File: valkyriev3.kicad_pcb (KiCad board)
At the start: 4 copper layers, 5 parts, among them J1 USB_C_Receptacle_USB2.0_16P, SW1 SW_SPST, SW2 SW_SPST, U1 ESP32-S3-MINI-1U, U2 MAX3232

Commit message: preliminary schematic wired, all footprints assigned, all laid out in PCB editor.
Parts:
- added BAT1: XH311HU-IV07E, Valkyrie_footprints:XH311HU-IV07E, F.Cu at (262.2, 44.2)
- added BZ1: Buzzer, Buzzer_Beeper:Buzzer_12x9.5RM7.6, F.Cu at (41.4, 116.8)
- added C1: 22 uF, Capacitor_SMD:C_0603_1608Metric, F.Cu at (41.7, 39.8)
- added C10: 10 uF, Capacitor_SMD:C_0603_1608Metric, F.Cu at (28.1, 179.7)
- added C11: 0.1 uF, Capacitor_SMD:C_0805_2012Metric, F.Cu at (23.8, 168.4)
- added C12: 0.1 uF, Capacitor_SMD:C_0805_2012Metric, F.Cu at (23.8, 171.4)
- added C13: 0.1 uF, Capacitor_SMD:C_0805_2012Metric, F.Cu at (23.8, 174.5)
- added C14: 0.1 uF, Capacitor_SMD:C_0805_2012Metric, F.Cu at (23.8, 177.5)
- added C15: 0.1 uF, Capacitor_SMD:C_0805_2012Metric, F.Cu at (23.8, 180.5)
- added C16: 0.1 uF, Capacitor_SMD:C_0805_2012Metric, F.Cu at (117.5, 127.1)
- added C17: 22 uF, Capacitor_SMD:C_0201_0603Metric, F.Cu at (109.7, 134.0)
- added C18: 22 uF, Capacitor_SMD:C_0201_0603Metric, F.Cu at (109.7, 135.8)
- added C19: 22 uF, Capacitor_SMD:C_0603_1608Metric, F.Cu at (115.9, 154.0)
- added C2: 22 uF, Capacitor_SMD:C_0603_1608Metric, F.Cu at (41.7, 42.3)
- added C20: 0.1 uF, Capacitor_SMD:C_0805_2012Metric, F.Cu at (120.1, 157.3)
- added C21: 0.1 uF, Capacitor_SMD:C_0805_2012Metric, F.Cu at (120.1, 160.3)
- added C22: 10 uF, Capacitor_SMD:C_0603_1608Metric, F.Cu at (115.9, 156.5)
- added C23: 22 uF, Capacitor_SMD:C_0603_1608Metric, F.Cu at (115.9, 159.0)
- added C24: 22 uF, Capacitor_SMD:C_0805_2012Metric, F.Cu at (105.0, 138.5)
- added C25: 10 uF, Capacitor_SMD:C_0805_2012Metric, F.Cu at (105.0, 141.5)
- added C26: 0.1 uF, Capacitor_SMD:C_0805_2012Metric, F.Cu at (105.0, 144.5)
- added C27: 0.1 uF, Capacitor_SMD:C_0805_2012Metric, F.Cu at (75.0, 174.9)
- added C28: 10 uF, Capacitor_SMD:C_0603_1608Metric, F.Cu at (79.2, 178.8)
- added C29: 0.1 uF, Capacitor_SMD:C_0805_2012Metric, F.Cu at (75.0, 177.9)
- added C3: 10 uF, Capacitor_SMD:C_0603_1608Metric, F.Cu at (41.7, 44.8)
- added C30: 0.1 uF, Capacitor_SMD:C_0805_2012Metric, F.Cu at (257.5, 43.0)
- added C31: 10 uF, Capacitor_SMD:C_0603_1608Metric, F.Cu at (269.3, 25.2)
- added C32: 22 uF, Capacitor_SMD:C_0603_1608Metric, F.Cu at (269.3, 27.8)
- added C33: 0.1 uF, Capacitor_SMD:C_0805_2012Metric, F.Cu at (257.5, 46.1)
- added C34: 220 uF, Capacitor_SMD:CP_Elec_6.3x7.7, F.Cu at (275.6, 83.2)
- added C35: 22 uF, Capacitor_SMD:C_0805_2012Metric, F.Cu at (272.6, 96.3)
- added C36: 10 uF, Capacitor_SMD:C_0603_1608Metric, F.Cu at (276.9, 96.0)
- added C37: 0.1 uF, Capacitor_SMD:C_0805_2012Metric, F.Cu at (272.6, 99.3)
- added C38: 0.1 uF, Capacitor_SMD:C_0805_2012Metric, F.Cu at (263.1, 140.9)
- added C39: 0.1 uF, Capacitor_SMD:C_0805_2012Metric, F.Cu at (263.1, 143.9)
- added C4: 0.1 uF, Capacitor_SMD:C_0805_2012Metric, F.Cu at (37.4, 40.0)
- added C40: 220 uF, Capacitor_SMD:CP_Elec_6.3x7.7, F.Cu at (134.6, 35.6)
- added C41: 220 uF, Capacitor_SMD:CP_Elec_6.3x7.7, F.Cu at (134.6, 43.7)
- added C42: 220 uF, Capacitor_SMD:CP_Elec_6.3x7.7, F.Cu at (134.6, 51.9)
- added C5: 0.1 uF, Capacitor_SMD:C_0805_2012Metric, F.Cu at (101.2, 79.2)
- added C6: 22 uF, Capacitor_SMD:C_0603_1608Metric, F.Cu at (101.1, 83.6)
- added C7: 0.1 uF, Capacitor_SMD:C_0603_1608Metric, F.Cu at (41.7, 49.8)
- added C8: 0.1 uF, Capacitor_SMD:C_0603_1608Metric, F.Cu at (41.7, 52.3)
- added C9: 22 uF, Capacitor_SMD:C_0603_1608Metric, F.Cu at (28.1, 177.2)
- added D1: NUP2105L, Package_TO_SOT_SMD:SOT-23, F.Cu at (22.4, 82.5)
- added D2: LED, LED_SMD:LED_0805_2012Metric, F.Cu at (41.5, 127.5)
- added D3: LED, LED_SMD:LED_0805_2012Metric, F.Cu at (41.5, 130.5)
- added D4: LED, LED_SMD:LED_0805_2012Metric, F.Cu at (41.5, 133.6)
- added D5: LED, LED_SMD:LED_0805_2012Metric, F.Cu at (133.1, 162.6)
- added D6: LED, LED_SMD:LED_0805_2012Metric, F.Cu at (122.7, 141.0)
- added D7: MSS1P3L, Diode_SMD:D_MicroSMP_AK, F.Cu at (267.6, 43.0)
- added D8: LED, LED_SMD:LED_0805_2012Metric, F.Cu at (269.6, 38.1)
- added D9: MMSZ4699T1G, Diode_SMD:D_SOD-123, F.Cu at (161.4, 33.2)
- added J10: Conn_01x03, Connector_PinHeader_2.54mm:PinHeader_1x03_P2.54mm_Vertical, F.Cu at (103.6, 19.8)
- added J11: Conn_01x03, Connector_PinHeader_2.54mm:PinHeader_1x03_P2.54mm_Vertical, F.Cu at (108.2, 19.8)
- added J2: DE9_Pins_MountingHoles, Connector_Dsub:DSUB-9_Pins_Horizontal_P2.77x2.84mm_EdgePinOffset7.70mm_Housed_MountingHolesOffset9.12mm, F.Cu at (27.6, 143.0)
- added J3: SMA_180C, Valkyrie_footprints:SMA_180C, F.Cu at (251.8, 45.3)
- added J4: SMA_180C, Valkyrie_footprints:SMA_180C, F.Cu at (274.5, 91.0)
- added J5: Conn_01x02_Socket, Connector_AMASS:AMASS_XT30PW-M_1x02_P2.50mm_Horizontal, F.Cu at (188.5, 31.6)
- added J6: Conn_01x02_Socket, Connector_AMASS:AMASS_XT30PW-M_1x02_P2.50mm_Horizontal, F.Cu at (154.9, 28.7)
- added J7: Conn_01x02_Socket, Connector_AMASS:AMASS_XT30PW-M_1x02_P2.50mm_Horizontal, F.Cu at (219.2, 31.6)
- added J8: Conn_01x03, Connector_PinHeader_2.54mm:PinHeader_1x03_P2.54mm_Vertical, F.Cu at (98.9, 19.8)
- added J9: Conn_01x05, Connector_PinHeader_2.54mm:PinHeader_1x05_P2.54mm_Vertical, F.Cu at (94.3, 19.8)
- added L1: 4.7 uH, Valkyrie_footprints:HPC 5020NF, F.Cu at (111.6, 142.1)
- added Q1: BC817, Package_TO_SOT_SMD:SOT-23, F.Cu at (29.7, 113.3)
- added Q2: BC817, Package_TO_SOT_SMD:SOT-23, F.Cu at (29.7, 117.9)
- added Q3: BC817, Package_TO_SOT_SMD:SOT-23, F.Cu at (29.7, 122.5)
- added Q4: BC817, Package_TO_SOT_SMD:SOT-23, F.Cu at (29.7, 127.2)
- added Q5: BC817, Package_TO_SOT_SMD:SOT-23, F.Cu at (267.3, 46.8)
- added Q6: DMP2305U, Package_TO_SOT_SMD:SOT-23, F.Cu at (146.9, 43.6)
- added Q7: DMG3420U, Package_TO_SOT_SMD:SOT-23, F.Cu at (195.8, 51.1)
- added Q8: DMG3420U, Package_TO_SOT_SMD:SOT-23, F.Cu at (195.8, 55.7)
- added R1: 10k, Resistor_SMD:R_0603_1608Metric, F.Cu at (45.7, 39.8)
- added R10: 1k, Resistor_SMD:R_0603_1608Metric, F.Cu at (36.4, 113.8)
- added R11: 1k, Resistor_SMD:R_0603_1608Metric, F.Cu at (36.4, 116.3)
- added R12: 1k, Resistor_SMD:R_0603_1608Metric, F.Cu at (36.4, 118.8)
- added R13: 1k, Resistor_SMD:R_0603_1608Metric, F.Cu at (36.4, 121.4)
- added R14: 1k, Resistor_SMD:R_0603_1608Metric, F.Cu at (36.4, 123.9)
- added R15: 1k, Resistor_SMD:R_0603_1608Metric, F.Cu at (36.4, 126.4)
- added R16: 10k, Resistor_SMD:R_0603_1608Metric, F.Cu at (113.2, 134.4)
- added R17: 1k, Resistor_SMD:R_0603_1608Metric, F.Cu at (115.9, 164.1)
- added R18: 1k, Resistor_SMD:R_0603_1608Metric, F.Cu at (117.3, 139.2)
- added R19: 52.3k, Resistor_SMD:R_0603_1608Metric, F.Cu at (117.3, 141.7)
- added R2: 10k, Resistor_SMD:R_0603_1608Metric, F.Cu at (45.7, 42.3)
- added R20: 10k, Resistor_SMD:R_0603_1608Metric, F.Cu at (117.3, 144.2)
- added R21: 1k, Resistor_SMD:R_0603_1608Metric, F.Cu at (269.3, 30.3)
- added R22: 1k, Resistor_SMD:R_0603_1608Metric, F.Cu at (269.3, 32.8)
- added R23: 1k, Resistor_SMD:R_0603_1608Metric, F.Cu at (269.3, 35.3)
- added R24: 1k, Resistor_SMD:R_0603_1608Metric, F.Cu at (200.3, 45.3)
- added R25: 100k, Resistor_SMD:R_0603_1608Metric, F.Cu at (200.3, 47.8)
- added R26: 100k, Resistor_SMD:R_0603_1608Metric, F.Cu at (151.4, 47.5)
- added R27: 1k, Resistor_SMD:R_0603_1608Metric, F.Cu at (200.3, 52.8)
- added R28: 100k, Resistor_SMD:R_0603_1608Metric, F.Cu at (200.3, 55.4)
- added R3: 5.1k, Resistor_SMD:R_0603_1608Metric, F.Cu at (35.3, 86.4)
- added R4: 5.1k, Resistor_SMD:R_0603_1608Metric, F.Cu at (35.3, 88.9)
- added R5: 100k, Resistor_SMD:R_0603_1608Metric, F.Cu at (45.7, 49.8)
- added R6: 10k, Resistor_SMD:R_0603_1608Metric, F.Cu at (45.7, 52.3)
- added R7: 10k, Resistor_SMD:R_0603_1608Metric, F.Cu at (45.7, 54.8)
- added R8: 54.9k, Resistor_SMD:R_0603_1608Metric, F.Cu at (45.7, 57.3)
- added R9: 1k, Resistor_SMD:R_0603_1608Metric, F.Cu at (36.4, 111.3)
- added U1: W25Q128JVS, Package_SO:SOIC-8_5.3x5.3mm_P1.27mm, F.Cu at (101.0, 90.2)
- added U10: LPS22HB, Package_LGA:ST_HLGA-10_2x2mm_P0.5mm_LayoutBorder3x2y, F.Cu at (262.7, 147.3)
- added U4: AMS1117-3.3, Package_TO_SOT_SMD:SOT-223-3_TabPin2, F.Cu at (127.3, 157.0)
- added U5: TPS562202, Package_TO_SOT_SMD:SOT-563, F.Cu at (119.2, 132.8)
- added U6: ~, Package_LGA:LGA-14_3x2.5mm_P0.5mm_LayoutBorder3x4y, F.Cu at (79.5, 175.5)
- added U7: ~, Valkyrie_footprints:Quectel_L86-M33, F.Cu at (257.6, 32.8)
- added U8: ~, Valkyrie_footprints:E22-400T33S, F.Cu at (256.7, 99.4)
- added U9: MS5607-02BA, Package_LGA:LGA-8_3x5mm_P1.25mm, F.Cu at (258.5, 142.9)
- moved U3 124.4 mm to (41.9, 171.4)
- moved SW1 67.8 mm to (31.6, 56.9)
- moved SW2 67.8 mm to (31.6, 62.1)
- moved U2 67.8 mm to (23.5, 45.8)
- moved J1 61.4 mm to (24.9, 94.5)
- renumbered U1 to U2, U2 to U3
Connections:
- net Net-(J1-VBUS-PadA4) renamed +5V
- J1 pad A1: Net-(J1-GND-PadA1) -> GND
- J1 pad A12: Net-(J1-GND-PadA1) -> GND
- J1 pad A5: unconnected-(J1-CC1-PadA5) -> /MCU/USB_CC1
- J1 pad A6: unconnected-(J1-D+-PadA6) -> /MCU/USB_DP
- J1 pad A7: unconnected-(J1-D--PadA7) -> /MCU/USB_DN
- J1 pad B1: Net-(J1-GND-PadA1) -> GND
- J1 pad B12: Net-(J1-GND-PadA1) -> GND
- J1 pad B5: unconnected-(J1-CC2-PadB5) -> /MCU/USB_CC2
- J1 pad B6: unconnected-(J1-D+-PadB6) -> /MCU/USB_DP
- J1 pad B7: unconnected-(J1-D--PadB7) -> /MCU/USB_DN
- J1 pad S1: unconnected-(J1-SHIELD-PadS1) -> GND
- SW1 pad 1: unconnected-(SW1-A-Pad1) -> GND
- SW1 pad 2: unconnected-(SW1-B-Pad2) -> /MCU/ESP_EN
- SW2 pad 1: unconnected-(SW2-A-Pad1) -> GND
- SW2 pad 2: unconnected-(SW2-B-Pad2) -> /MCU/ESP_BOOT
- U2 pad 1: Net-(U1-GND-Pad1) -> GND
- U2 pad 10: unconnected-(U1-IO6-Pad10) -> OUT_MAIN
- U2 pad 11: unconnected-(U1-IO7-Pad11) -> OUT_DROGUE
- U2 pad 12: unconnected-(U1-IO8-Pad12) -> LORA_AUX
- U2 pad 13: unconnected-(U1-IO9-Pad13) -> LORA_RESET
- U2 pad 14: unconnected-(U1-IO10-Pad14) -> ESP_SDA
- U2 pad 15: unconnected-(U1-IO11-Pad15) -> ESP_SCL
- U2 pad 16: unconnected-(U1-IO12-Pad16) -> ESP_TXD2
- U2 pad 17: unconnected-(U1-IO13-Pad17) -> ESP_RXD2
- U2 pad 18: unconnected-(U1-IO14-Pad18) -> BAT_LEVEL
- U2 pad 19: unconnected-(U1-IO15-Pad19) -> LORA_M0
- U2 pad 2: Net-(U1-GND-Pad1) -> GND
- U2 pad 20: unconnected-(U1-IO16-Pad20) -> LORA_M1
- U2 pad 21: unconnected-(U1-IO17-Pad21) -> ESP_TXD1
- U2 pad 22: unconnected-(U1-IO18-Pad22) -> EXP_RXD1
- U2 pad 23: unconnected-(U1-USB_D--Pad23) -> /MCU/USB_DN
- U2 pad 24: unconnected-(U1-USB_D+-Pad24) -> /MCU/USB_DP
- U2 pad 28: unconnected-(U1-IO33-Pad28) -> SPI_HOLD
- U2 pad 29: unconnected-(U1-IO34-Pad29) -> SPI_CS1
- U2 pad 3: unconnected-(U1-3V3-Pad3) -> +3V3
- U2 pad 31: unconnected-(U1-IO35-Pad31) -> SPI_MISO
- U2 pad 32: unconnected-(U1-IO36-Pad32) -> SPI_SCLK
- U2 pad 33: unconnected-(U1-IO37-Pad33) -> SPI_MOSI
- U2 pad 34: unconnected-(U1-IO38-Pad34) -> SPI_WP
- U2 pad 36: unconnected-(U1-IO40-Pad36) -> ESP_TXD2
- U2 pad 37: unconnected-(U1-IO41-Pad37) -> ESP_RXD2
- U2 pad 38: unconnected-(U1-IO42-Pad38) -> GPS_RESET
- U2 pad 39: unconnected-(U1-TXD0-Pad39) -> ESP_TXD0
- U2 pad 4: unconnected-(U1-IO0-Pad4) -> /MCU/ESP_BOOT
- U2 pad 40: unconnected-(U1-RXD0-Pad40) -> ESP_RXD0
- U2 pad 42: Net-(U1-GND-Pad1) -> GND
- U2 pad 43: Net-(U1-GND-Pad1) -> GND
- U2 pad 45: unconnected-(U1-EN-Pad45) -> /MCU/ESP_EN
- U2 pad 46: Net-(U1-GND-Pad1) -> GND
- U2 pad 47: Net-(U1-GND-Pad1) -> GND
- U2 pad 48: Net-(U1-GND-Pad1) -> GND
- U2 pad 49: Net-(U1-GND-Pad1) -> GND
- U2 pad 5: unconnected-(U1-IO1-Pad5) -> LED_MAIN
- U2 pad 50: Net-(U1-GND-Pad1) -> GND
- U2 pad 51: Net-(U1-GND-Pad1) -> GND
- U2 pad 52: Net-(U1-GND-Pad1) -> GND
- U2 pad 53: Net-(U1-GND-Pad1) -> GND
- U2 pad 54: Net-(U1-GND-Pad1) -> GND
- U2 pad 55: Net-(U1-GND-Pad1) -> GND
- U2 pad 56: Net-(U1-GND-Pad1) -> GND
- U2 pad 57: Net-(U1-GND-Pad1) -> GND
- U2 pad 58: Net-(U1-GND-Pad1) -> GND
- U2 pad 59: Net-(U1-GND-Pad1) -> GND
- U2 pad 6: unconnected-(U1-IO2-Pad6) -> LED_DROGUE
- U2 pad 60: Net-(U1-GND-Pad1) -> GND
- U2 pad 61: Net-(U1-GND-Pad1) -> GND
- U2 pad 62: Net-(U1-GND-Pad1) -> GND
- U2 pad 63: Net-(U1-GND-Pad1) -> GND
- U2 pad 64: Net-(U1-GND-Pad1) -> GND
- U2 pad 65: Net-(U1-GND-Pad1) -> GND
- U2 pad 8: unconnected-(U1-IO4-Pad8) -> BUZZER
- U2 pad 9: unconnected-(U1-IO5-Pad9) -> LED_USER
- U3 pad 1: unconnected-(U2-C1+-Pad1) -> /MCU/MAX323_C1+
- U3 pad 10: unconnected-(U2-T2IN-Pad10) -> ESP_TXD0
- U3 pad 15: unconnected-(U2-GND-Pad15) -> GND
- U3 pad 16: unconnected-(U2-VCC-Pad16) -> +3V3
- U3 pad 2: unconnected-(U2-VS+-Pad2) -> /MCU/MAX323_VS+
- U3 pad 3: unconnected-(U2-C1--Pad3) -> /MCU/MAX323_C1-
- U3 pad 4: unconnected-(U2-C2+-Pad4) -> /MCU/MAX323_C2+
- U3 pad 5: unconnected-(U2-C2--Pad5) -> /MCU/MAX323_C2-
- U3 pad 6: unconnected-(U2-VS--Pad6) -> /MCU/MAX323_VS-
- U3 pad 7: unconnected-(U2-T2OUT-Pad7) -> /MCU/RS232_TXD
- U3 pad 8: unconnected-(U2-R2IN-Pad8) -> /MCU/RS232_RXD
- U3 pad 9: unconnected-(U2-R2OUT-Pad9) -> ESP_RXD0

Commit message: reassigned some footprints, preliminary PCB layout
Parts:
- C11, C12, C13, C14, C15, C16, C20, C21, C27, C29, C30, C33, C35, C37, C38, C39, C4, C5: footprint Capacitor_SMD:C_0805_2012Metric -> Capacitor_SMD:C_0603_1608Metric
- C17, C18: footprint Capacitor_SMD:C_0201_0603Metric -> Capacitor_SMD:C_0603_1608Metric
- D2, D3, D4, D5, D6, D8: footprint LED_SMD:LED_0805_2012Metric -> LED_SMD:LED_0603_1608Metric
- moved C39 175.7 mm to (103.7, 69.9), turned to 90 degrees
- moved U9 173.8 mm to (101.1, 69.1), turned to 180 degrees
- moved R22 142.4 mm to (136.7, 84.5)
- moved R21 142.1 mm to (136.6, 81.2)
- moved C31 141.7 mm to (139.3, 81.7), turned to -90 degrees
- moved D8 141.3 mm to (136.6, 86.0), turned to 180 degrees
- moved C36 139.8 mm to (137.1, 100.3)
- moved J4 138.8 mm to (146.0, 143.4), turned to -90 degrees
- moved C32 138.0 mm to (139.4, 74.1), turned to 90 degrees
- moved D7 137.1 mm to (136.5, 82.8)
- moved C34 136.9 mm to (139.1, 92.1)
- moved C35 135.6 mm to (137.1, 98.8)
- moved R23 135.4 mm to (143.0, 84.1), turned to 90 degrees
- moved C37 134.8 mm to (137.8, 102.8), turned to 90 degrees
- moved C38 133.5 mm to (131.2, 120.2), turned to 90 degrees
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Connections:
- D1 pad 1: /MCU/USB_DP -> /MCU/USB_DN
- D1 pad 2: /MCU/USB_DN -> /MCU/USB_DP
- J11 pad 1: ESP_TXD0 -> ESP_RXD0
- J11 pad 2: ESP_RXD0 -> ESP_TXD0
- J8 pad 1: ESP_TXD1 -> ESP_TXD2
- J8 pad 2: EXP_RXD1 -> EXP_RXD2
- J9 pad 4: ESP_TXD2 -> ESP_TXD1
- J9 pad 5: ESP_RXD2 -> ESP_RXD1
- U2 pad 16: ESP_TXD2 -> unconnected-(U2-IO12-Pad16)
- U2 pad 17: ESP_RXD2 -> unconnected-(U2-IO13-Pad17)
- U7 pad 1: ESP_TXD1 -> ESP_TXD2
- U7 pad 2: EXP_RXD1 -> EXP_RXD2
- U8 pad 4: ESP_TXD2 -> ESP_TXD1
- U8 pad 5: ESP_RXD2 -> ESP_RXD1
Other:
- board outline added: 70 x 100 mm

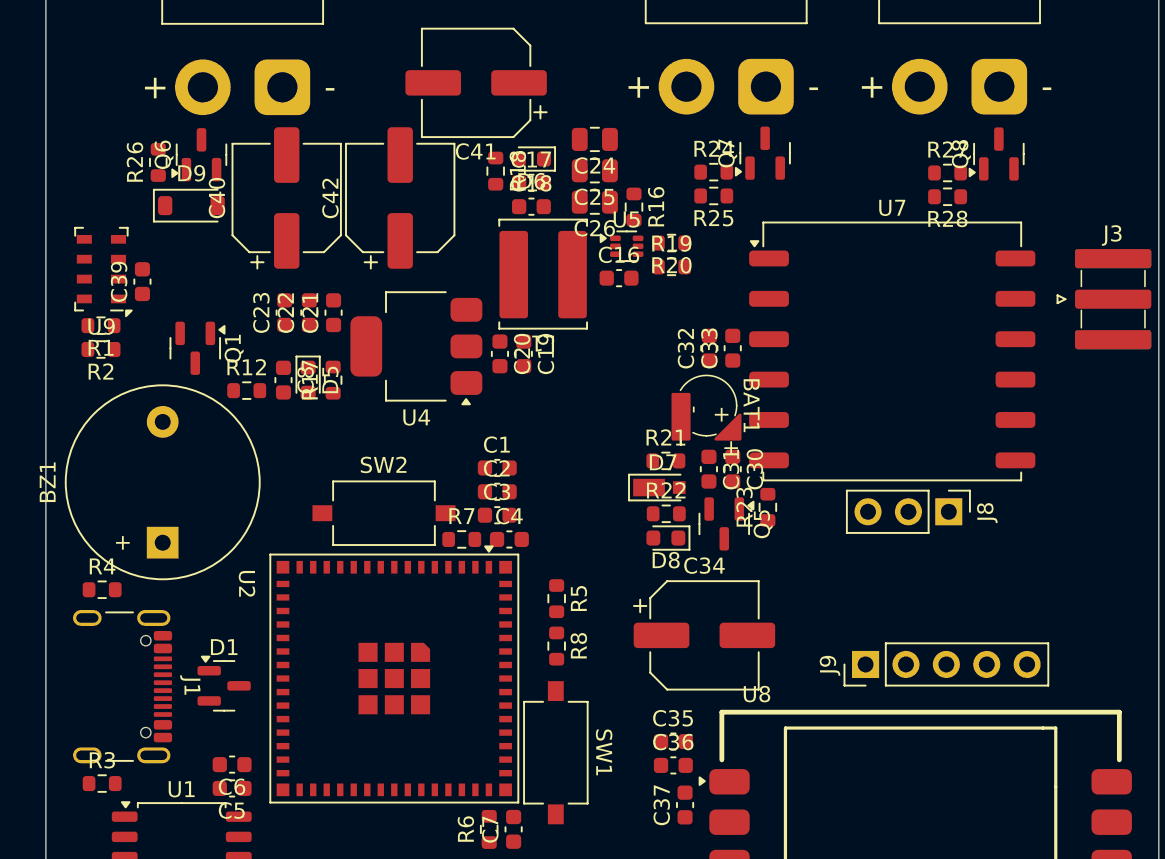
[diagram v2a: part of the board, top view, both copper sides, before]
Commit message: added missing output diodes, added 3d models, misc. re-laying
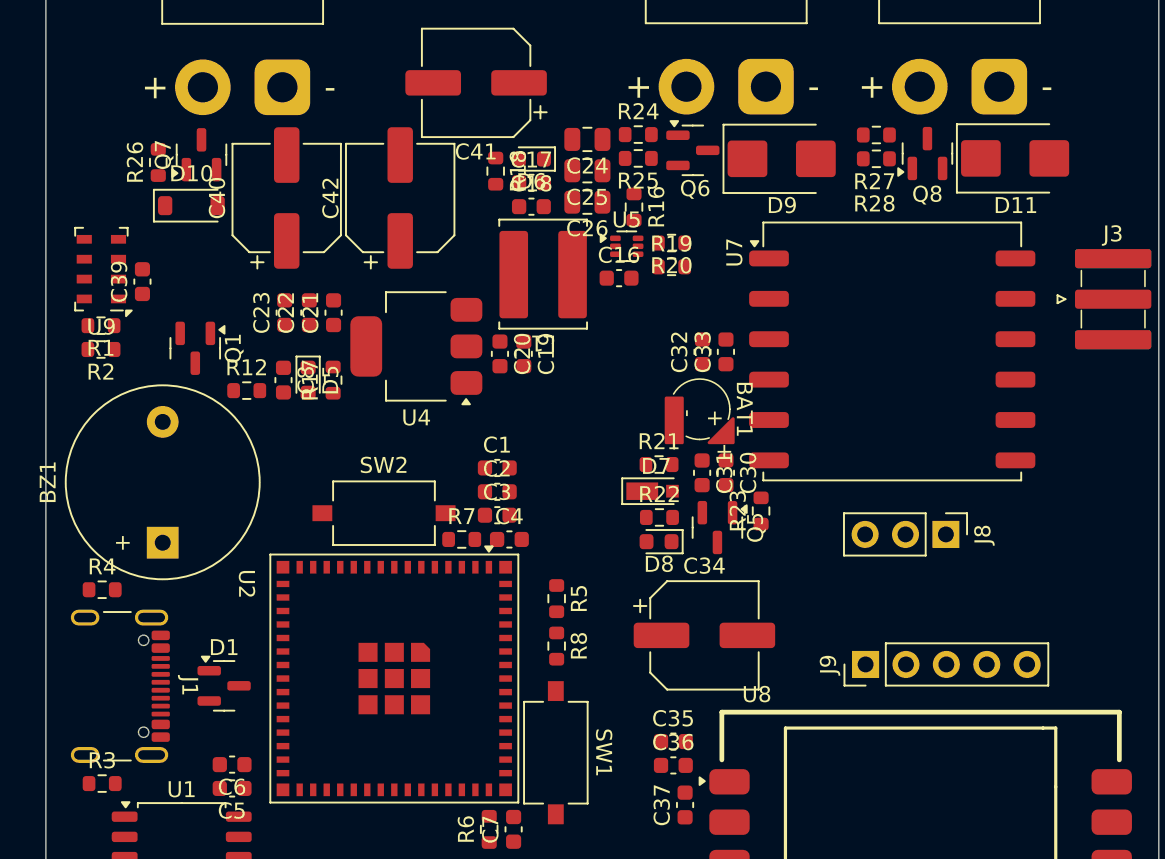
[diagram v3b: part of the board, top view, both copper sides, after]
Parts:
- added D11: S2A, Diode_SMD:D_SMB, F.Cu at (158.6, 62.1)
- added D9: S2A, Diode_SMD:D_SMB, F.Cu at (143.9, 62.2)
- moved R24 5.30 mm to (134.9, 60.6)
- moved R25 5.30 mm to (134.9, 62.1)
- moved R28 5.07 mm to (149.9, 62.2)
- moved R27 5.07 mm to (149.9, 60.7)
- moved Q6 4.55 mm to (138.3, 61.6), turned to 0 degrees
- moved Q8 4.49 mm to (153.1, 61.8)
- moved J8 1.43 mm to (154.2, 85.8)
- moved BAT1 0.49 mm to (138.8, 77.9)
- moved C31 0.49 mm to (138.9, 81.9)
- moved C32 0.49 mm to (138.9, 74.3)
- moved R22 0.49 mm to (136.2, 84.7)
- moved C30 0.49 mm to (140.4, 81.9)
- moved C33 0.49 mm to (140.4, 74.3)
- moved D7 0.49 mm to (136.0, 83.1)
- moved D8 0.49 mm to (136.2, 86.2)
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- renumbered D9 to D10, Q7 to Q6, Q6 to Q7
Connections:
- J5 pad 1: /Connectors/MAIN_D -> /Connectors/MAIN_ANODE
- J7 pad 1: /Connectors/DROGUE_D -> /Connectors/DROGUE_ANODE
- J8 pad 2: EXP_RXD2 -> ESP_RXD2
- U2 pad 22: EXP_RXD1 -> ESP_RXD1
- U7 pad 2: EXP_RXD2 -> ESP_RXD2

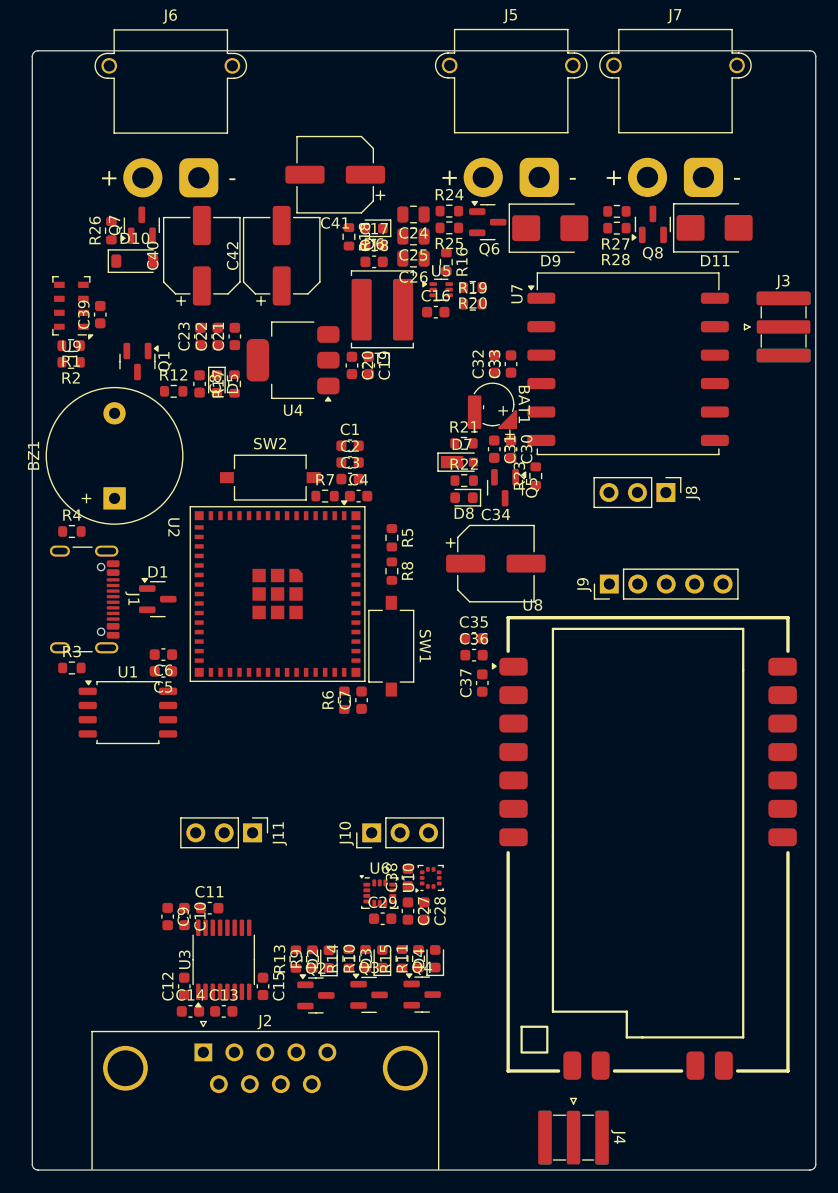
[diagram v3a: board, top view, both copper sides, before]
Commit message: revision of layout. added 3d model of the card
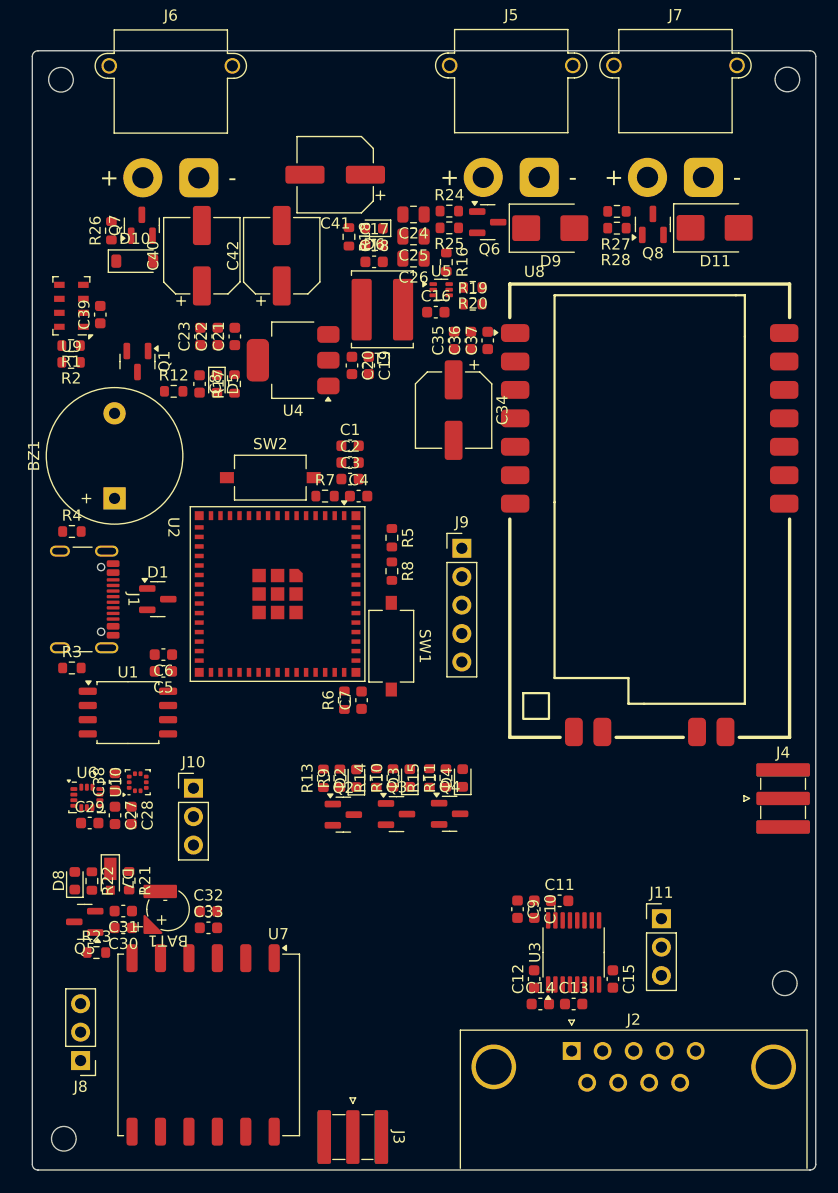
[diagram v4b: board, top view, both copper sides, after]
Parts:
- added H1: MountingHole, MountingHole:MountingHole_2.2mm_M2, F.Cu at (100.2, 48.9)
- added H2: MountingHole, MountingHole:MountingHole_2.2mm_M2, F.Cu at (165.1, 48.9)
- added H3: MountingHole, MountingHole:MountingHole_2.2mm_M2, F.Cu at (164.9, 129.6)
- added H4: MountingHole, MountingHole:MountingHole_2.2mm_M2, F.Cu at (100.5, 143.5)
- moved J3 82.0 mm to (126.3, 143.4), turned to -90 degrees
- moved J8 72.9 mm to (102.0, 136.5), turned to 180 degrees
- moved U7 71.5 mm to (113.4, 135.1), turned to -90 degrees
- moved R23 57.9 mm to (103.4, 126.9), turned to 0 degrees
- moved C33 57.2 mm to (113.4, 124.7), turned to 0 degrees
- moved C32 55.2 mm to (113.4, 123.2), turned to 0 degrees
- moved C30 55.0 mm to (105.8, 124.7), turned to 180 degrees
- moved Q5 54.0 mm to (102.3, 124.1), turned to 180 degrees
- moved BAT1 53.6 mm to (109.8, 123.0), turned to 180 degrees
- moved C31 52.9 mm to (105.8, 123.2), turned to 180 degrees
- moved R21 49.2 mm to (106.3, 120.5), turned to -90 degrees
- moved R22 48.9 mm to (103.0, 120.5), turned to -90 degrees
- moved D8 48.8 mm to (101.4, 120.5), turned to 90 degrees
- moved D7 48.7 mm to (104.6, 120.3), turned to -90 degrees
- moved J11 37.3 mm to (153.8, 123.9), turned to 0 degrees
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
